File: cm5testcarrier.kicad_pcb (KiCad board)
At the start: 4 copper layers, 173 x 129 mm, 15 parts, among them J1 Barrel_Jack, J2 Conn_02x20_Odd_Even, SW1 SW_Wuerth_450301014042, U1 MagJack-A70-112-331N126, U2 GL2576-5.0SF8DR

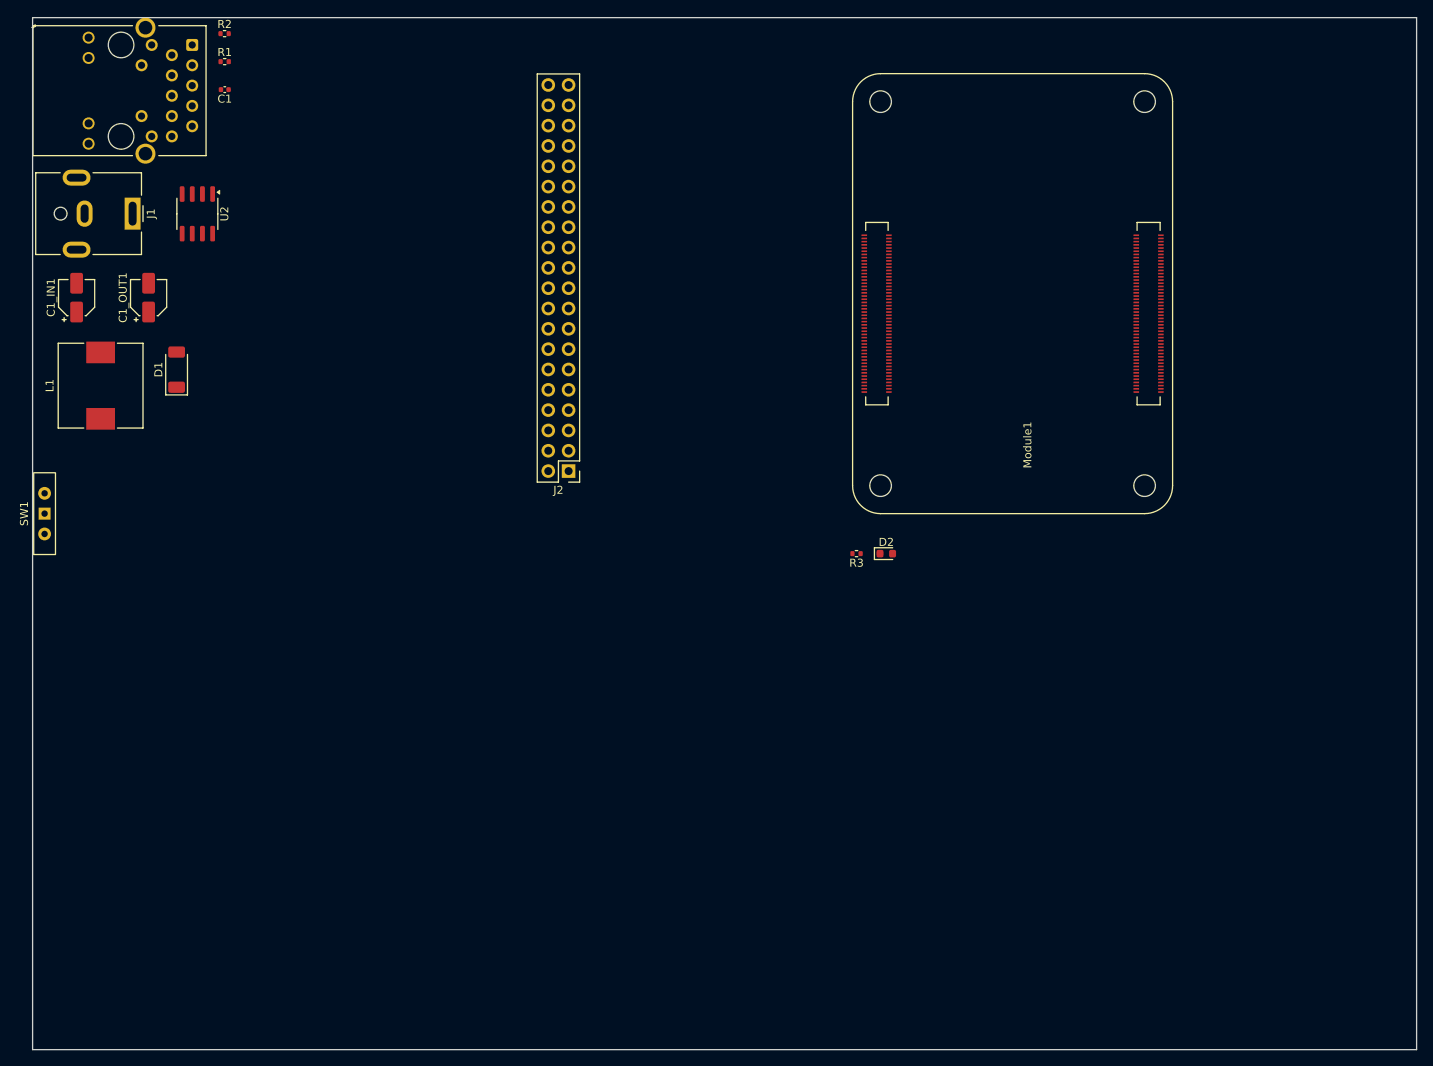
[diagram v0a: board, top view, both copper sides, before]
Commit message: Servo Controller Finished miscs things reorganized
 - implemented Servo Controller
 - split servo voltage supplies
 - corrected gpio connections
 - implemented fan connector
 - made the usb 2.0 more tidy
 - cleaned up pin nets
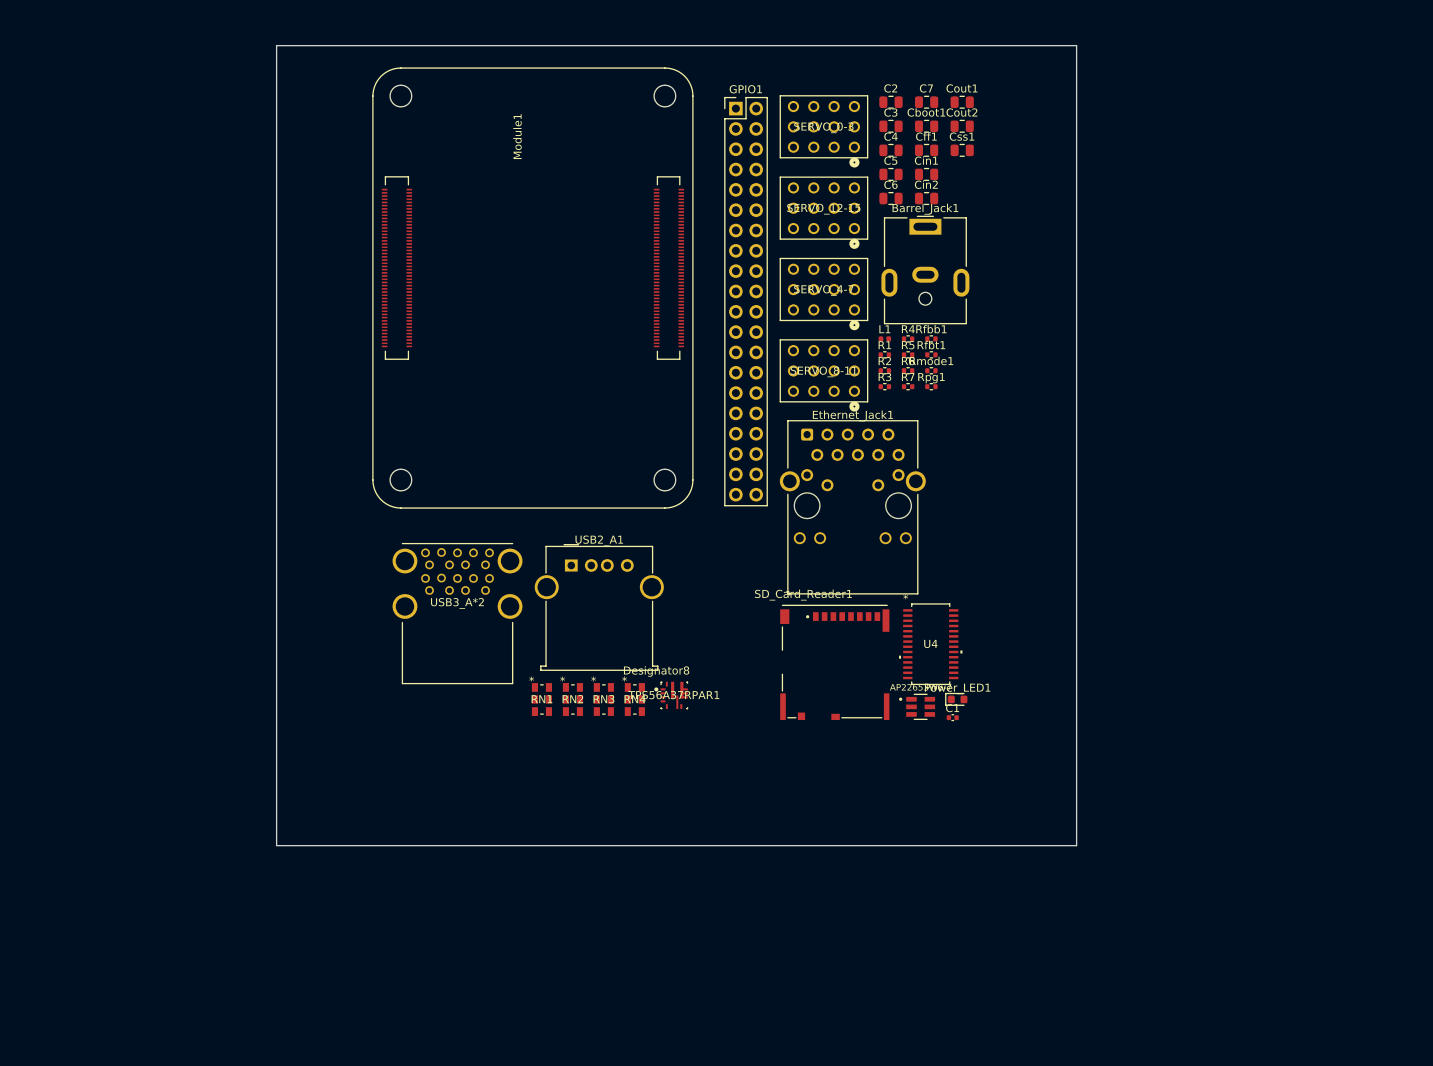
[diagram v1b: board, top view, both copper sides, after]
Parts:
- removed C1_IN1: 100uF, Capacitor_SMD:CP_Elec_4x5.8
- removed C1_OUT1: 680uF, Capacitor_SMD:CP_Elec_4x5.8
- removed D1: 1N5822, Diode_SMD:D_SOD-128
- removed D2: LED Red, LED_SMD:LED_0603_1608Metric
- removed J1: Barrel_Jack, Connector_BarrelJack:BarrelJack_CUI_PJ-063AH_Horizontal
- removed J2: Conn_02x20_Odd_Even, Connector_PinHeader_2.54mm:PinHeader_2x20_P2.54mm_Vertical
- removed SW1: SW_Wuerth_450301014042, Button_Switch_THT:SW_Slide-03_Wuerth-WS-SLTV_10x2.5x6.4_P2.54mm
- removed U1: MagJack-A70-112-331N126, CM5IO:TRJG0926HENL
- removed U2: GL2576-5.0SF8DR, Package_SO:SOIC-8_3.9x4.9mm_P1.27mm
- added AP22653W6-7: U3, AP22653W6_7 USB curernt limit switch:SOT95P280X145-6N, F.Cu at (170.0, 122.2)
- added Barrel_Jack1: Barrel_Jack, Connector_BarrelJack:BarrelJack_CUI_PJ-063AH_Horizontal, F.Cu at (170.6, 62.1)
- added C2: 10u, Capacitor_SMD:C_0805_2012Metric, F.Cu at (166.3, 46.6)
- added C3: 10u, Capacitor_SMD:C_0805_2012Metric, F.Cu at (166.3, 49.6)
- added C4: 100uF, Capacitor_SMD:C_0805_2012Metric, F.Cu at (166.3, 52.6)
- added C5: 10u, Capacitor_SMD:C_0805_2012Metric, F.Cu at (166.3, 55.6)
- added C6: 10u, Capacitor_SMD:C_0805_2012Metric, F.Cu at (166.3, 58.6)
- added C7: 10uF, Capacitor_SMD:C_0805_2012Metric, F.Cu at (170.8, 46.6)
- added Cboot1: 150 pF, Capacitor_SMD:C_0805_2012Metric, F.Cu at (170.8, 49.6)
- added Cff1: 150 pF, Capacitor_SMD:C_0805_2012Metric, F.Cu at (170.8, 52.6)
- added Cin1: 10uf, Capacitor_SMD:C_0805_2012Metric, F.Cu at (170.8, 55.6)
- added Cin2: 10uf, Capacitor_SMD:C_0805_2012Metric, F.Cu at (170.8, 58.6)
- added Cout1: 22 nF, Capacitor_SMD:C_0805_2012Metric, F.Cu at (175.2, 46.6)
- added Cout2: 22 nF, Capacitor_SMD:C_0805_2012Metric, F.Cu at (175.2, 49.6)
- added Css1: 22 nF, Capacitor_SMD:C_0805_2012Metric, F.Cu at (175.2, 52.6)
- added Ethernet_Jack1: MagJack-A70-112-331N126, CM5IO:TRJG0926HENL, F.Cu at (161.5, 97.0)
- added GPIO1: Conn_02x20_Odd_Even, Connector_PinHeader_2.54mm:PinHeader_2x20_P2.54mm_Vertical, F.Cu at (146.9, 47.4)
- added Power_LED1: D2, LED_SMD:LED_0603_1608Metric, F.Cu at (174.6, 121.2)
- added R4: 10k 1%, Resistor_SMD:R_0402_1005Metric, F.Cu at (168.4, 76.2)
- added R5: 10K, Resistor_SMD:R_0402_1005Metric, F.Cu at (168.4, 78.2)
- added R6: 10K, Resistor_SMD:R_0402_1005Metric, F.Cu at (168.4, 80.1)
- added R7: 10K, Resistor_SMD:R_0402_1005Metric, F.Cu at (168.4, 82.1)
- added RN1: 220, 220 ohm resistor net CAY16:BO_CAY16-L, F.Cu at (122.7, 121.2)
- added RN2: 220, 220 ohm resistor net CAY16:BO_CAY16-L, F.Cu at (126.5, 121.2)
- added RN3: 220, 220 ohm resistor net CAY16:BO_CAY16-L, F.Cu at (130.4, 121.2)
- added RN4: 220, 220 ohm resistor net CAY16:BO_CAY16-L, F.Cu at (134.3, 121.2)
- added Rfbb1: 10 kΩ, Resistor_SMD:R_0402_1005Metric, F.Cu at (171.3, 76.2)
- added Rfbt1: 73.2 kΩ, Resistor_SMD:R_0402_1005Metric, F.Cu at (171.3, 78.2)
- added Rmode1: 52.3 kΩ, Resistor_SMD:R_0402_1005Metric, F.Cu at (171.3, 80.1)
- added Rpg1: 100kΩ, Resistor_SMD:R_0402_1005Metric, F.Cu at (171.3, 82.1)
- added SD_Card_Reader1: Micro_SD_Card_Det2, CM5IO:SDCARD_MOLEX_503398-1892, F.Cu at (159.3, 116.5)
- added SERVO_0-3: HEADER-3X04, 12pin header:CON12_3X4_TU_TSW_SAI, F.Cu at (157.9, 49.7)
- added SERVO_12-15: HEADER-3X04, 12pin header:CON12_3X4_TU_TSW_SAI, F.Cu at (157.9, 59.8)
- added SERVO_4-7: HEADER-3X04, 12pin header:CON12_3X4_TU_TSW_SAI, F.Cu at (157.9, 70.0)
- added SERVO_8-11: HEADER-3X04, 12pin header:CON12_3X4_TU_TSW_SAI, F.Cu at (157.9, 80.2)
- added TPS56A37RPAR1: TPS56A37RPAR, TPS56A37:RPA0010A-MFG, F.Cu at (139.2, 120.7)
- added U4: PCA9685, PCA9685:TSSOP28_SOT361-1_NXP-L, F.Cu at (171.3, 114.3)
- added USB2_A1: J2, Connector_USB:USB_A_Molex_67643_Horizontal, F.Cu at (126.3, 104.5)
- added USB3_A*2: J3, CM5IO:MTCONN_UBAF30-D2011, F.Cu at (112.1, 109.6)
- L1: value 100uH -> 3.3 µH; footprint Inductor_SMD:L_10.4x10.4_H4.8 -> Inductor_SMD:L_0402_1005Metric
- moved C1 120.2 mm to (174.0, 123.5), turned to 0 degrees
- moved L1 98.2 mm to (165.5, 76.2), turned to 0 degrees
- moved R2 92.7 mm to (165.5, 80.1)
- moved R1 90.3 mm to (165.5, 78.2)
- moved Module1 55.7 mm to (138.0, 45.8), turned to 180 degrees
- moved R3 21.2 mm to (165.5, 82.1), turned to 0 degrees
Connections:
- net -12V renamed GND
- L1 pad 2: Net-(D1-K) -> +5V
- Module1 pad 103: unconnected-(Module1B-USB2_N-Pad103) -> /USB_2_N
- Module1 pad 105: unconnected-(Module1B-USB2_P-Pad105) -> /USB_2_P
- Module1 pad 111: unconnected-(Module1B-VBUS_EN-Pad111) -> /VBUS_EN
- Module1 pad 130: unconnected-(Module1B-USB3-0-RX_P-Pad130) -> /USB3-0-RX_P
- Module1 pad 134: unconnected-(Module1B-USB3-0-D_P-Pad134) -> /USB3-0-D_P
- Module1 pad 136: unconnected-(Module1B-USB3-0-D_N-Pad136) -> /USB3-0-D_N
- Module1 pad 140: unconnected-(Module1B-USB3-0-TX_N-Pad140) -> /USB3-0-TX_N
- Module1 pad 142: unconnected-(Module1B-USB3-0-TX_P-Pad142) -> /USB3-0-TX_P
- Module1 pad 157: unconnected-(Module1B-USB3-1-RX_N-Pad157) -> /USB3-1-RX_N
- Module1 pad 159: unconnected-(Module1B-USB3-1-RX_P-Pad159) -> /USB3-1-RX_P
- Module1 pad 16: unconnected-(Module1A-FAN_TACHO-Pad16) -> /FAN_TACHOMETER
- Module1 pad 163: unconnected-(Module1B-USB3-1-D_P-Pad163) -> /USB3-1-D_P
- Module1 pad 165: unconnected-(Module1B-USB3-1-D_N-Pad165) -> /USB3-1-D_N
- Module1 pad 169: unconnected-(Module1B-USB3-1-TX_N-Pad169) -> /USB3-1-TX_N
- Module1 pad 171: unconnected-(Module1B-USB3-1-TX_P-Pad171) -> /USB3-1-TX_P
- Module1 pad 19: unconnected-(Module1A-FAN_PWM-Pad19) -> /FAN_PWM
- Module1 pad 25: unconnected-(Module1A-GPIO21-Pad25) -> /GPIO21
- Module1 pad 27: unconnected-(Module1A-GPIO20-Pad27) -> /GPIO20
- Module1 pad 29: unconnected-(Module1A-GPIO16-Pad29) -> /GPIO16
- Module1 pad 31: unconnected-(Module1A-GPIO12-Pad31) -> /GPIO12
- Module1 pad 35: unconnected-(Module1A-ID_SC-Pad35) -> /GPIO1
- Module1 pad 36: unconnected-(Module1A-ID_SD-Pad36) -> /GPIO0
- Module1 pad 37: unconnected-(Module1A-GPIO7-Pad37) -> /GPIO7
- Module1 pad 39: unconnected-(Module1A-GPIO8-Pad39) -> /GPIO8
- Module1 pad 41: unconnected-(Module1A-GPIO25-Pad41) -> /GPIO25
- Module1 pad 45: unconnected-(Module1A-GPIO24-Pad45) -> /GPIO24
- Module1 pad 47: unconnected-(Module1A-GPIO23-Pad47) -> /GPIO23
- Module1 pad 49: unconnected-(Module1A-GPIO18-Pad49) -> /GPIO18
- Module1 pad 51: unconnected-(Module1A-GPIO15-Pad51) -> /GPIO15
- Module1 pad 55: unconnected-(Module1A-GPIO14-Pad55) -> /GPIO14
- Module1 pad 57: unconnected-(Module1A-SD_CLK-Pad57) -> /SD_CLK
- Module1 pad 61: unconnected-(Module1A-SD_DAT3-Pad61) -> /SD_DAT3
- Module1 pad 63: unconnected-(Module1A-SD_DAT0-Pad63) -> /SD_DAT0
- Module1 pad 67: unconnected-(Module1A-SD_DAT1-Pad67) -> /SD_DAT1
- Module1 pad 69: unconnected-(Module1A-SD_DAT2-Pad69) -> /SD_DAT2
- Module1 pad 75: unconnected-(Module1A-SD_PWR_ON-Pad75) -> /SD_PWR_ON
- Module1 pad 78: unconnected-(Module1A-GPIO_VREF(1.8v/3.3v_Input)-Pad78) -> +3V3
- Module1 pad 80: unconnected-(Module1A-SCL0-Pad80) -> /PCA_SCL
- Module1 pad 82: unconnected-(Module1A-SDA0-Pad82) -> /PCA_SDA
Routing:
- net Net-(C1-Pad2): track 0.71 -> 0.00 mm
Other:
- board size 173 x 129 mm -> 100 x 100 mm

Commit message: Updated footprints & reorganized file structure
 - changed footprints to hand solderable sizes
 - made the file structure make more sense
 - removed files that were not needed in the project
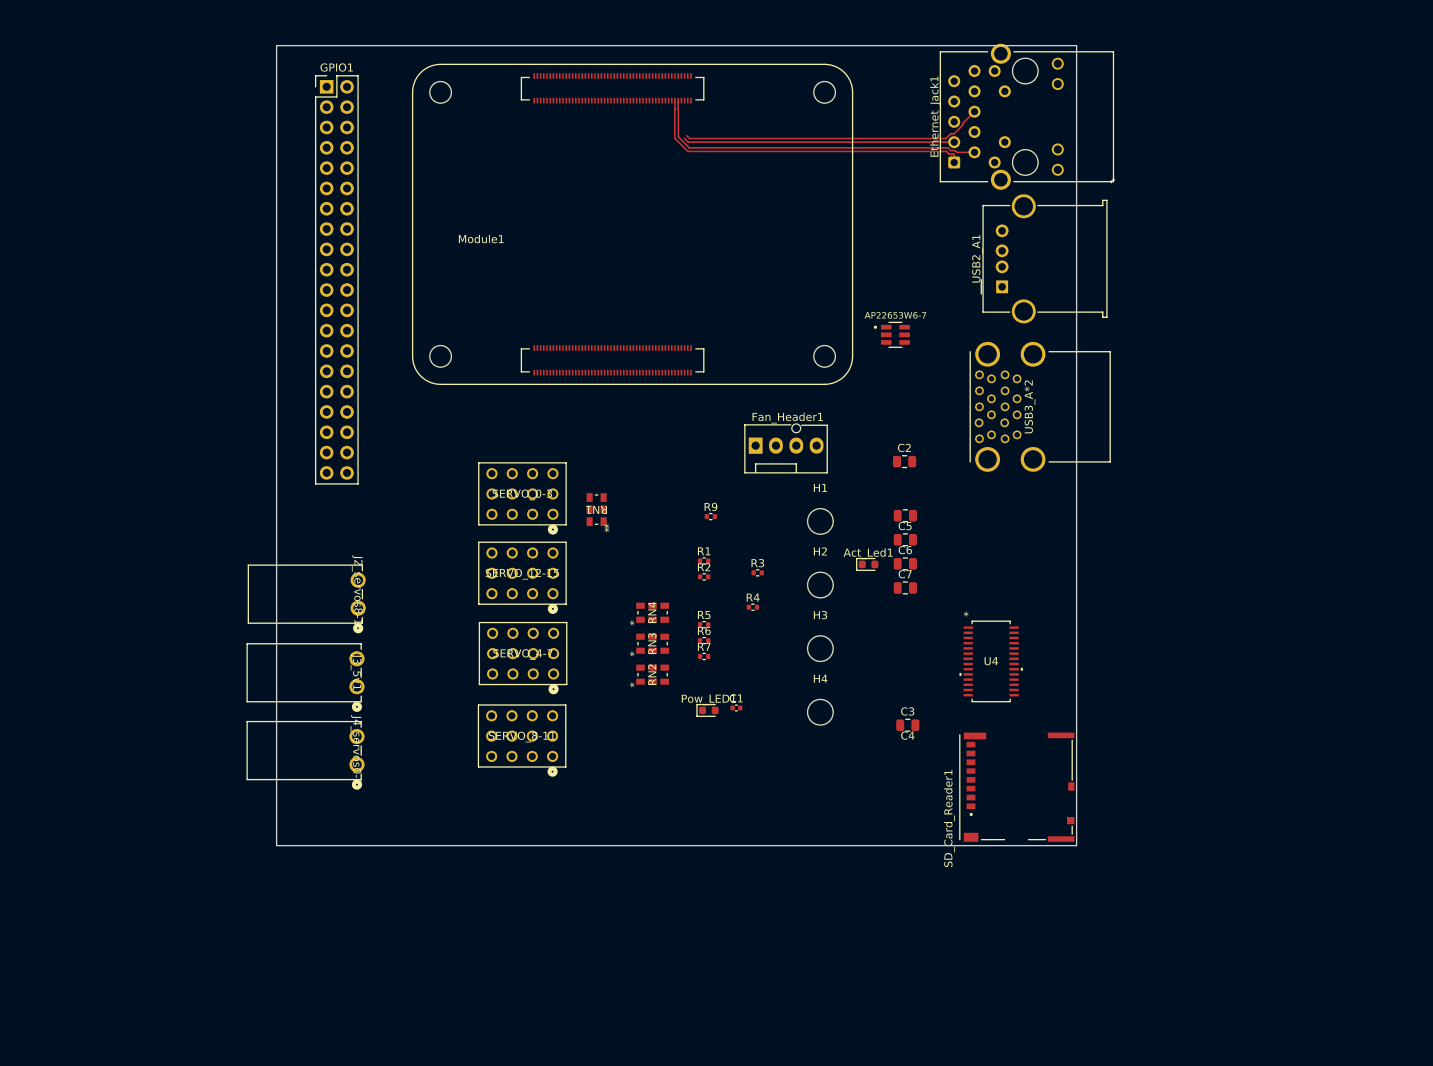
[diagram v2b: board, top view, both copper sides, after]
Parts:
- removed Barrel_Jack1: Barrel_Jack, Connector_BarrelJack:BarrelJack_CUI_PJ-063AH_Horizontal
- removed Cboot1, Cff1: 150 pF, Capacitor_SMD:C_0805_2012Metric
- removed Cin1, Cin2: 10uf, Capacitor_SMD:C_0805_2012Metric
- removed Cout1, Cout2, Css1: 22 nF, Capacitor_SMD:C_0805_2012Metric
- removed L1: 3.3 µH, Inductor_SMD:L_0402_1005Metric
- removed Power_LED1: D2, LED_SMD:LED_0603_1608Metric
- removed Rfbb1: 10 kΩ, Resistor_SMD:R_0402_1005Metric
- removed Rfbt1: 73.2 kΩ, Resistor_SMD:R_0402_1005Metric
- removed Rmode1: 52.3 kΩ, Resistor_SMD:R_0402_1005Metric
- removed Rpg1: 100kΩ, Resistor_SMD:R_0402_1005Metric
- removed TPS56A37RPAR1: TPS56A37RPAR, TPS56A37:RPA0010A-MFG
- added Act_Led1: D2, LED_SMD:LED_0603_1608Metric, F.Cu at (163.5, 104.3)
- added Fan_Header1: Conn_01x04_Pin, Connector:FanPinHeader_1x04_P2.54mm_Vertical, F.Cu at (149.4, 89.5)
- added H1: M3, MountingHole:MountingHole_3.2mm_M3, F.Cu at (157.5, 99.0)
- added H2: M3, MountingHole:MountingHole_3.2mm_M3, F.Cu at (157.5, 106.9)
- added H3: M3, MountingHole:MountingHole_3.2mm_M3, F.Cu at (157.5, 114.9)
- added H4: M3, MountingHole:MountingHole_3.2mm_M3, F.Cu at (157.5, 122.8)
- added J2_servos8-15: 2091-1372, RoboSubCompute.footprints:CONN2_2091-1372_WAGO, F.Cu at (99.7, 109.8)
- added J3_5v1: 2091-1372, RoboSubCompute.footprints:CONN2_2091-1372_WAGO, F.Cu at (99.5, 119.6)
- added J4_servos0-7: 2091-1372, RoboSubCompute.footprints:CONN2_2091-1372_WAGO, F.Cu at (99.5, 129.4)
- added Pow_LED1: D1, LED_SMD:LED_0603_1608Metric, F.Cu at (143.5, 122.6)
- added R9: 1k, Resistor_SMD:R_0402_1005Metric, F.Cu at (143.8, 98.4)
- AP22653W6-7: footprint AP22653W6_7 USB curernt limit switch:SOT95P280X145-6N -> RoboSubCompute.footprints:USB_Current_limit_Switch_AP22653W6-7
- Ethernet_Jack1: footprint CM5IO:TRJG0926HENL -> RoboSubCompute.footprints:ethernet_jack
- Module1: footprint CM5IO:Raspberry-Pi-5-Compute-Module -> RoboSubCompute.footprints:Raspberry-Pi-5-Compute-Module
- RN1, RN2, RN3, RN4: footprint 220 ohm resistor net CAY16:BO_CAY16-L -> RoboSubCompute.footprints:4x_220_resistor_net
- SD_Card_Reader1: footprint CM5IO:SDCARD_MOLEX_503398-1892 -> RoboSubCompute.footprints:SDCARD_MOLEX_503398-1892
- SERVO_0-3, SERVO_12-15, SERVO_4-7, SERVO_8-11: footprint 12pin header:CON12_3X4_TU_TSW_SAI -> RoboSubCompute.footprints:CON12_3X4_TU_TSW_SAI
- U4: footprint PCA9685:TSSOP28_SOT361-1_NXP-L -> RoboSubCompute.footprints:servo_controller_pca9685
- USB3_A*2: footprint CM5IO:MTCONN_UBAF30-D2011 -> RoboSubCompute.footprints:USB3.0_2x_conn
- moved USB3_A*2 76.2 mm to (184.1, 84.7), turned to 90 degrees
- moved C3 74.9 mm to (168.4, 124.5)
- moved USB2_A1 64.1 mm to (180.2, 69.7), turned to 90 degrees
- moved C7 60.8 mm to (168.1, 107.3)
- moved SERVO_0-3 59.4 mm to (120.2, 95.5)
- moved SERVO_8-11 59.2 mm to (120.2, 125.8)
- moved SERVO_12-15 59.2 mm to (120.2, 105.5)
- moved SERVO_4-7 59.0 mm to (120.3, 115.5)
- moved Ethernet_Jack1 53.2 mm to (183.1, 48.4), turned to 90 degrees
- moved GPIO1 51.2 mm to (95.8, 44.6)
- moved AP22653W6-7 46.6 mm to (166.9, 75.7)
- moved C5 45.7 mm to (168.1, 101.3)
- moved C4 45.7 mm to (168.1, 98.3)
- moved C6 45.7 mm to (168.1, 104.3)
- moved C2 45.0 mm to (168.0, 91.5)
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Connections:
- net Net-(Module1A-LED_nPWR) renamed /Power_LED
- net Net-(SERVO_0-3-Pad11) renamed +Servo 0-7 voltage
- net Net-(SERVO_12-15-Pad11) renamed +Servo 8-15 voltage
- Module1 pad 113: unconnected-(Module1B-GND-Pad113) -> GND
- Module1 pad 21: unconnected-(Module1A-LED_nACT-Pad21) -> /Act_LED
- Module1 pad 59: unconnected-(Module1A-GND-Pad59) -> GND
- Module1 pad 89: unconnected-(Module1A-WiFi_nDisable-Pad89) -> /Disable_wifi
- Module1 pad 91: unconnected-(Module1A-BT_nDisable-Pad91) -> /Disable_bt
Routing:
- net /p-0: track 0.00 -> 42.4 mm
- net /p+0: track 0.00 -> 41.5 mm
- net /p-1: track 0.00 -> 37.7 mm
- net /p+1: track 0.00 -> 34.0 mm
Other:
- copper layers 4 -> 2
